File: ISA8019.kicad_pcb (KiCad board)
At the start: 2 copper layers, 157.4 x 74.2 mm, 55 parts, among them J1 Bus_ISA_16bit, J2 8P8C_Shielded, J4 JP, J5 PNP force, J6 BROM size and base address, J7 I/O base address, J8 Medium type, J9 IRQ select, T1 13F-39MNL, U1 RTL8019AS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

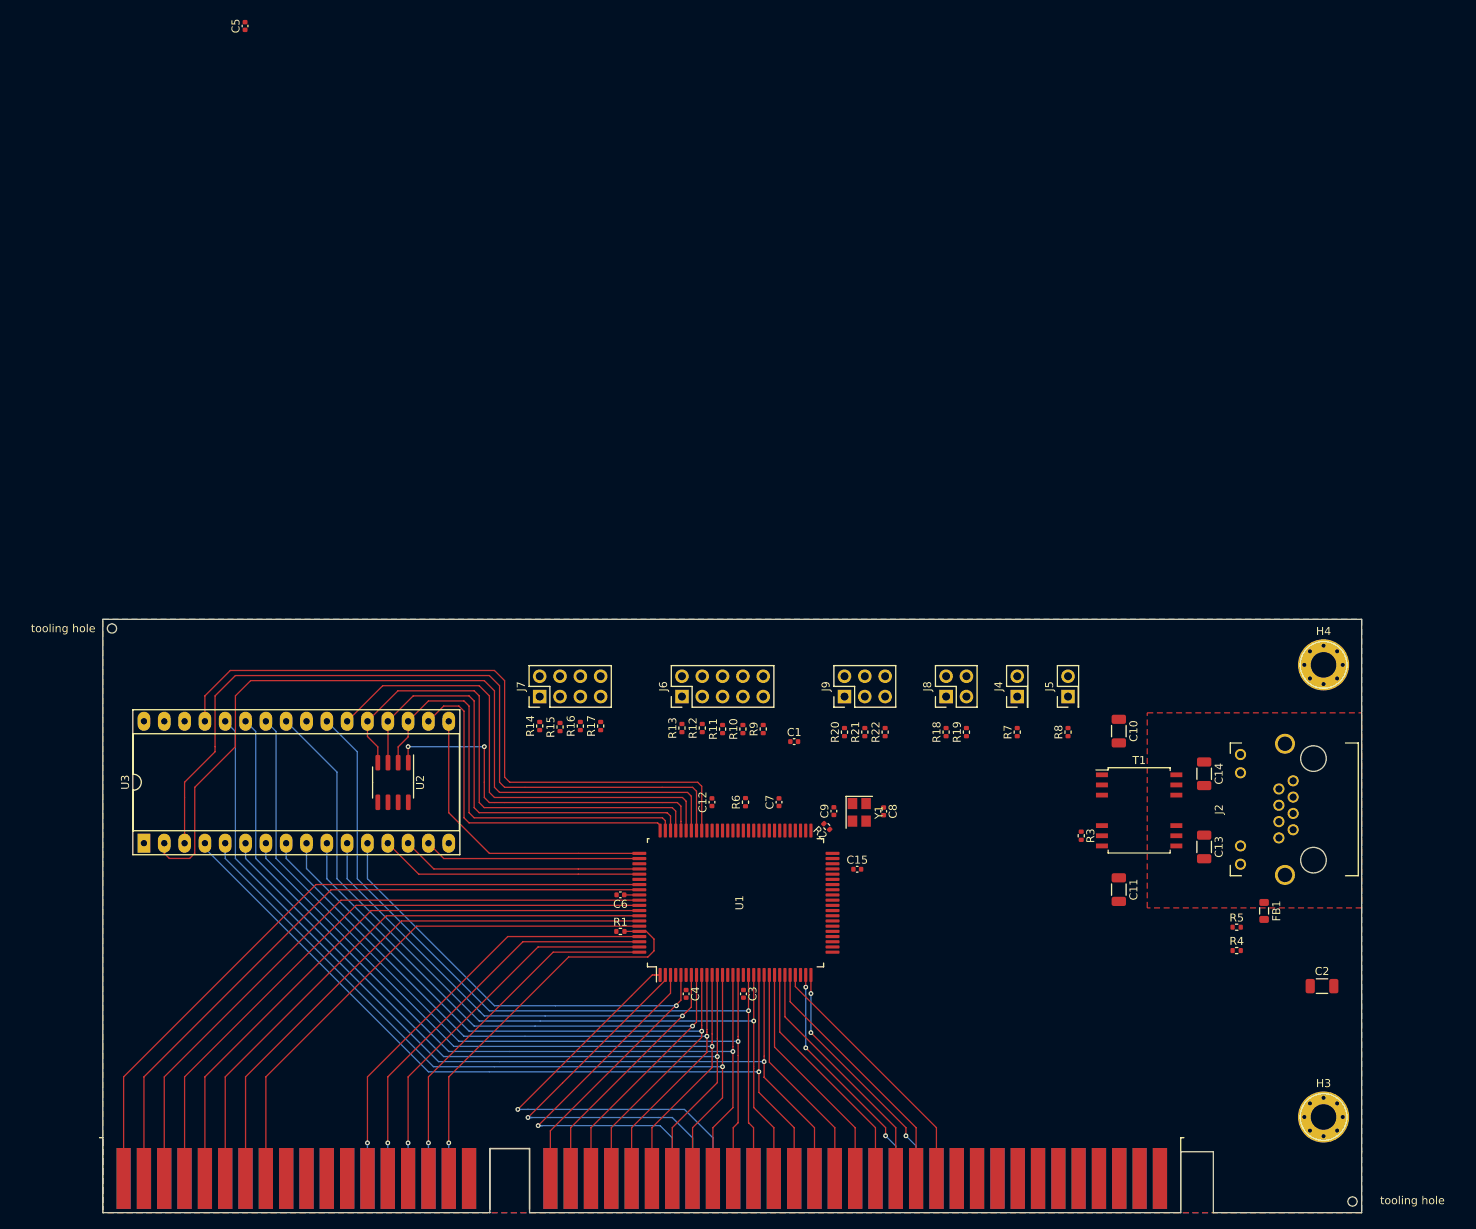
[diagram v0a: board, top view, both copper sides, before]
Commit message: Route all nets
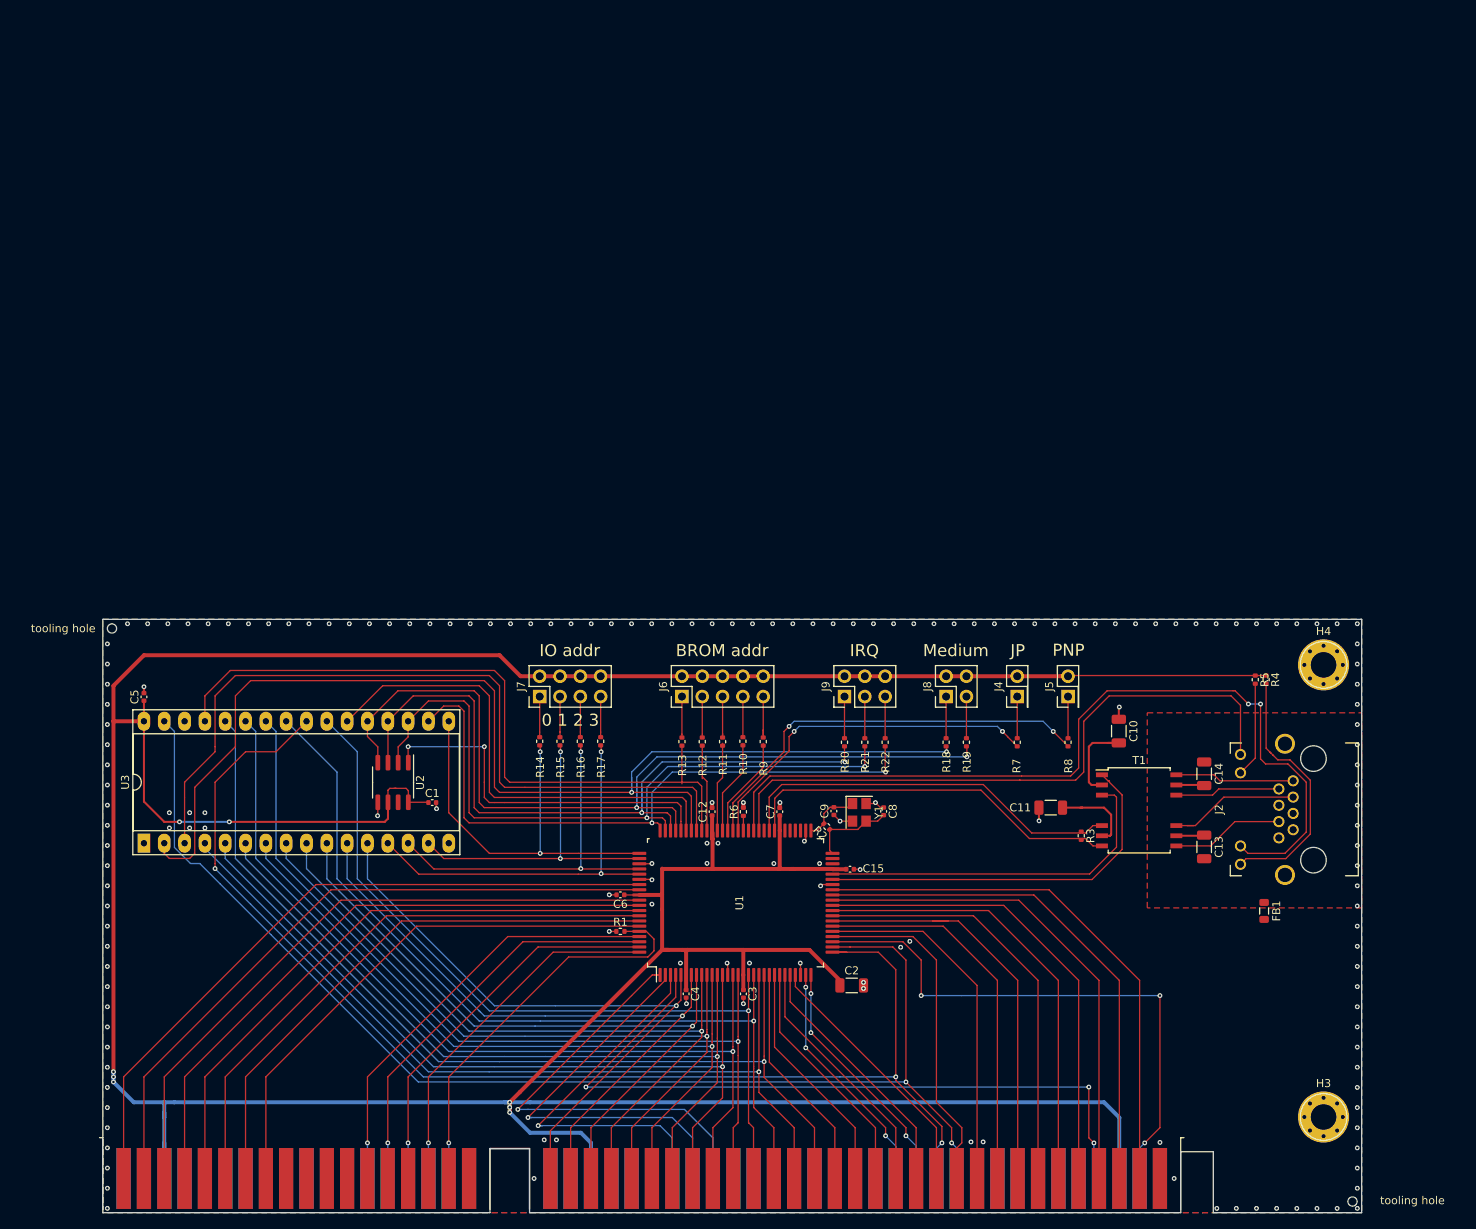
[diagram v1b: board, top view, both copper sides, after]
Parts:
- moved C5 84.8 mm to (40.7, 99.1)
- moved C2 58.8 mm to (129.2, 135.2)
- moved C1 45.9 mm to (76.7, 112.3)
- moved R4 34.1 mm to (181.0, 96.9), turned to 270 degrees
- moved R5 31.0 mm to (179.6, 96.9), turned to 270 degrees
- moved C11 13.3 mm to (154.0, 112.9), turned to 180 degrees
- moved R14 1.91 mm to (90.2, 104.6)
- moved R16 1.91 mm to (95.2, 104.6)
- moved R17 1.91 mm to (97.8, 104.6)
- moved R15 1.78 mm to (92.7, 104.7)
- moved R13 1.69 mm to (108.0, 104.7)
- moved R12 1.69 mm to (110.5, 104.7)
- moved R11 1.57 mm to (113.0, 104.7)
- moved R9 1.57 mm to (118.1, 104.7)
- moved R10 1.52 mm to (115.6, 104.6)
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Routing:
- net +5V: track 1.98 -> 539.9 mm, vias 0 -> 8
- net /~ISA_SMEMR: track 0.00 -> 161.8 mm, vias 0 -> 3
- net /~ISA_SMEMW: track 0.00 -> 159.7 mm, vias 0 -> 2
- net /LED1: track 0.00 -> 107.4 mm, vias 0 -> 2
- net /ISA_IRQ2: track 0.00 -> 93.5 mm, vias 0 -> 3
- net /LED0: track 0.00 -> 80.3 mm
- net /ISA_RESET: track 0.00 -> 70.2 mm, vias 0 -> 3
- net /ISA_D7: track 0.00 -> 67.8 mm
- net /ISA_D6: track 0.00 -> 65.0 mm
- net /ISA_D5: track 0.00 -> 62.2 mm
- net /ISA_D4: track 0.00 -> 59.4 mm
- net /ISA_D3: track 0.00 -> 56.6 mm
- net /ISA_D2: track 0.00 -> 53.8 mm
- net /ISA_D1: track 0.00 -> 52.9 mm
- net /PNP: track 0.00 -> 52.4 mm, vias 0 -> 2
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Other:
- board text added: "0 1 2 3"
- board text added: "BROM addr"
- board text added: "IO addr"
- board text added: "IRQ"
- board text added: "JP"
- board text added: "Medium"
- board text added: "PNP"

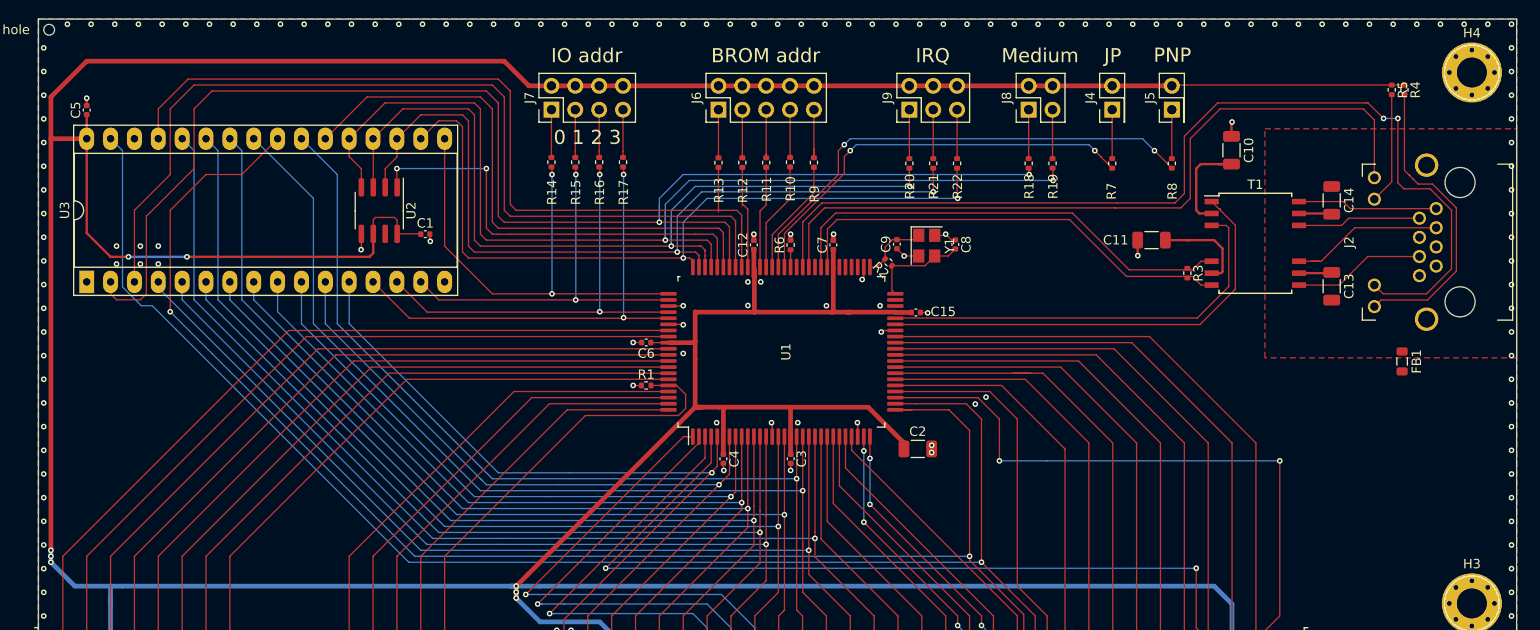
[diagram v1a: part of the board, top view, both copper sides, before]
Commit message: Add silkscreen and jumper settings
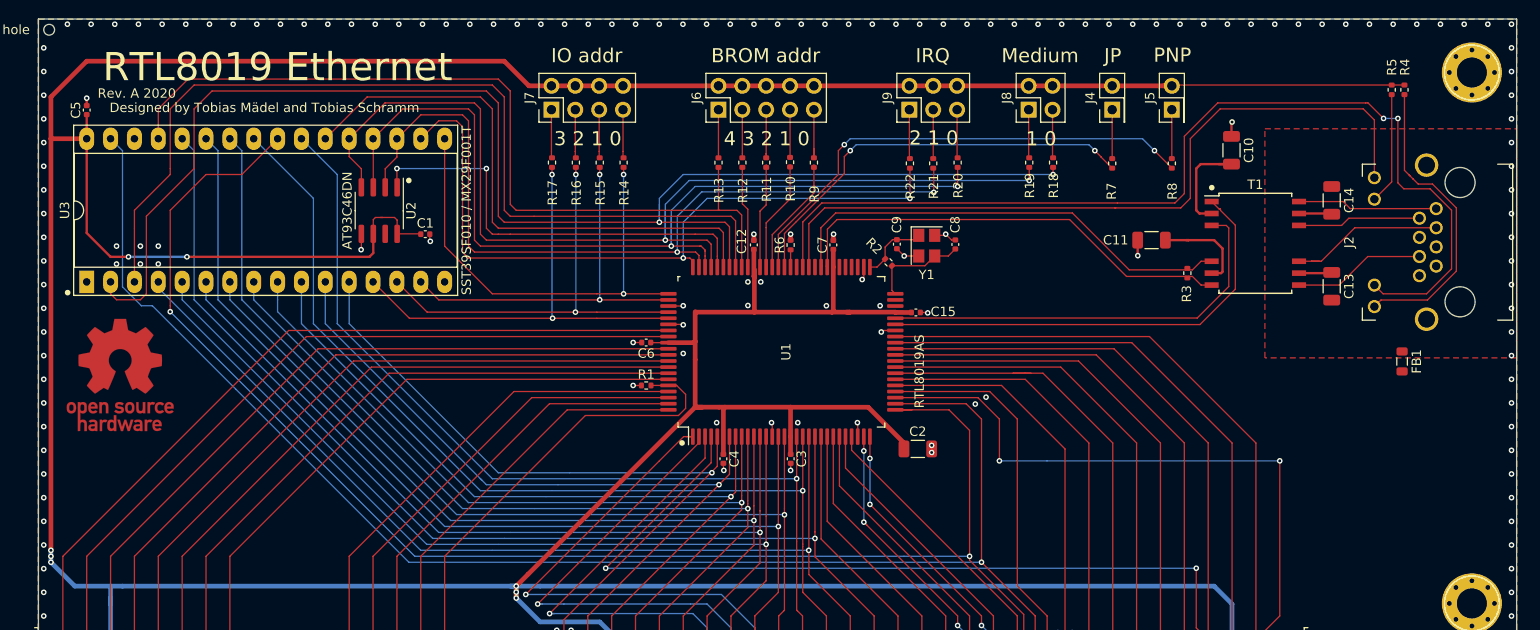
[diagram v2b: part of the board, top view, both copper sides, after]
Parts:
- added REF**: OSHW-Logo_11.4x12mm_Copper, Symbol:OSHW-Logo_11.4x12mm_Copper, F.Cu at (44.3, 127.3)
- J4: value JP -> Jumper mode
- moved R14 7.68 mm to (97.8, 104.7)
- moved R17 7.56 mm to (90.2, 104.7)
- moved R20 5.14 mm to (133.4, 104.7)
- moved R22 5.02 mm to (128.3, 104.8)
- moved R15 2.60 mm to (95.3, 104.7)
- moved R18 2.60 mm to (143.6, 104.7)
- moved R19 2.48 mm to (141.0, 104.7)
- moved R16 2.48 mm to (92.8, 104.7)
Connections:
- R14 pad 2: Net-(J7-Pad1) -> Net-(J7-Pad7)
- R15 pad 2: Net-(J7-Pad3) -> Net-(J7-Pad5)
- R16 pad 2: Net-(J7-Pad5) -> Net-(J7-Pad3)
- R17 pad 2: Net-(J7-Pad7) -> Net-(J7-Pad1)
- R18 pad 2: Net-(J8-Pad1) -> Net-(J8-Pad3)
- R19 pad 2: Net-(J8-Pad3) -> Net-(J8-Pad1)
- R20 pad 2: Net-(J9-Pad1) -> Net-(J9-Pad5)
- R22 pad 2: Net-(J9-Pad5) -> Net-(J9-Pad1)
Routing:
- net /BD6: track 93.1 -> 98.2 mm
- net /BD4: track 81.7 -> 76.6 mm
- net /BA14: track 148.1 -> 150.7 mm
- net /BD7: track 112.9 -> 110.6 mm
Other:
- board text added: "- Jumper-mode (disable PnP) - Force Plug'n'Play (ignore EEPROM settings)"
- board text added: "1 0"
- board text added: "2 1 0"
- board text added: "3 2 1 0"
- board text added: "4 3 2 1 0"
- board text added: "Boot ROM size & address 4 3 2 1 0 0 0 X X X Disabled 0 1 0 0 0 C000H, 32K 0 1 0 0 1 C800H, 32K 0 1 0 1 0 D000H, 32K 0 1 0 1 1 D800H, 32K 0 1 1 0 0 C000H, 64K 0 1 1 0 1 D000H, 64K 1 0 0 0 0 C000H, 16K 1 0 0 0 1 C400H, 16K 1 0 0 1 0 C800H, 16K 1 0 0 1 1 CC00H, 16K 1 0 1 0 0 D000H, 16K 1 0 1 0 1 D400H, 16K 1 0 1 1 0 D800H, 16K 1 0 1 1 1 DC00H, 16K 1 1 0 0 0 C000H, Paged 1 1 0 0 1 C400H, Paged 1 1 0 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"
- board text added: "Designed by Tobias Mädel and Tobias Schramm"
- board text added: "I/O address 3 2 1 0 0 0 0 0 300H 0 0 0 1 320H 0 0 1 0 340H 0 0 1 1 360H 1 0 0 0 380H 1 0 0 1 3A0H 1 0 1 0 3C0H 1 0 1 1 3E0H 0 1 0 0 200H 0 1 0 1 220H 0 1 1 0 240H 0 1 1 1 260H 1 1 0 0 280H 1 1 0 1 2A0H 1 1 1 0 2C0H 1 1 1 1 2E0H"
- board text added: "IRQ 2 1 0 0 0 0 IRQ2 0 0 1 IRQ3 0 1 0 IRQ4 0 1 1 IRQ5 1 0 0 IRQ10 1 0 1 IRQ11 1 1 0 IRQ12 1 1 1 IRQ15"
- board text added: "JP PNP Set no jumpers for PnP mode"
- board text added: "Medium type 1 0 0 0 10BaseT w/ link test 0 1 10BaseT w/o link test 1 0 10Base5 1 1 10Base2"
- board text added: "RTL8019 Ethernet"
- board text added: "Rev. A 2020"
- board text added: "tbspace.de"
- board text removed: "0 1 2 3"

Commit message: Add JLC markings, manufacturing details and new gerbers
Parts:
- removed REF**: OSHW-Logo_11.4x12mm_Copper, Symbol:OSHW-Logo_11.4x12mm_Copper
- added H5: OSHW Logo, Symbol:OSHW-Logo_11.4x12mm_Copper, F.Cu at (44.5, 127.5)
- J1: footprint Connector_PCBEdge:BUS_AT -> Bus_AT_without_Silkscreen:BUS_AT_WO_SILKSCREEN
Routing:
- net GND: track 27.1 -> 46.4 mm, vias 173 -> 218
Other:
- board text added: "JLCJLCJLCJLC"
- board text added: "JP PNP Set no jumpers for PnP mode NE2000-compatible"
- board text removed: "JP PNP Set no jumpers for PnP mode"

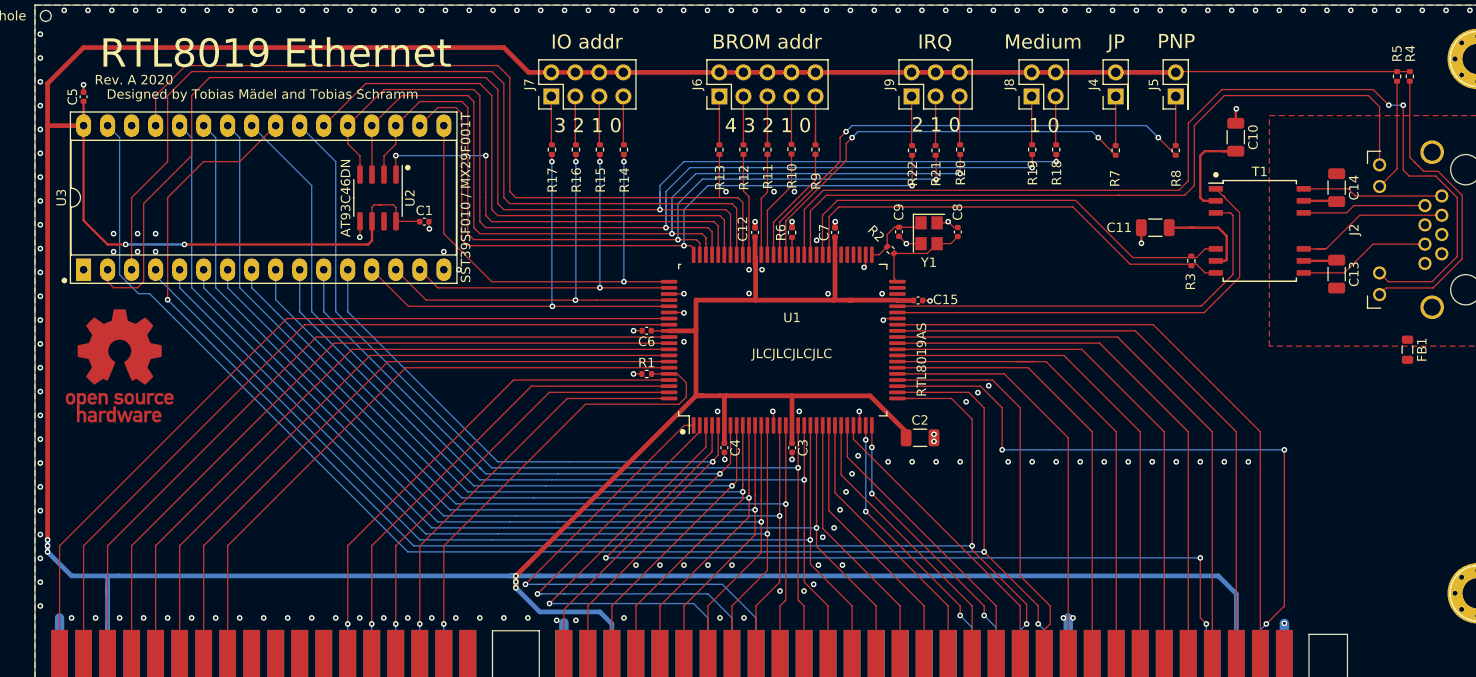
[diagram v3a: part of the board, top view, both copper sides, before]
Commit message: More GND via stitching and minor aesthetic fixes
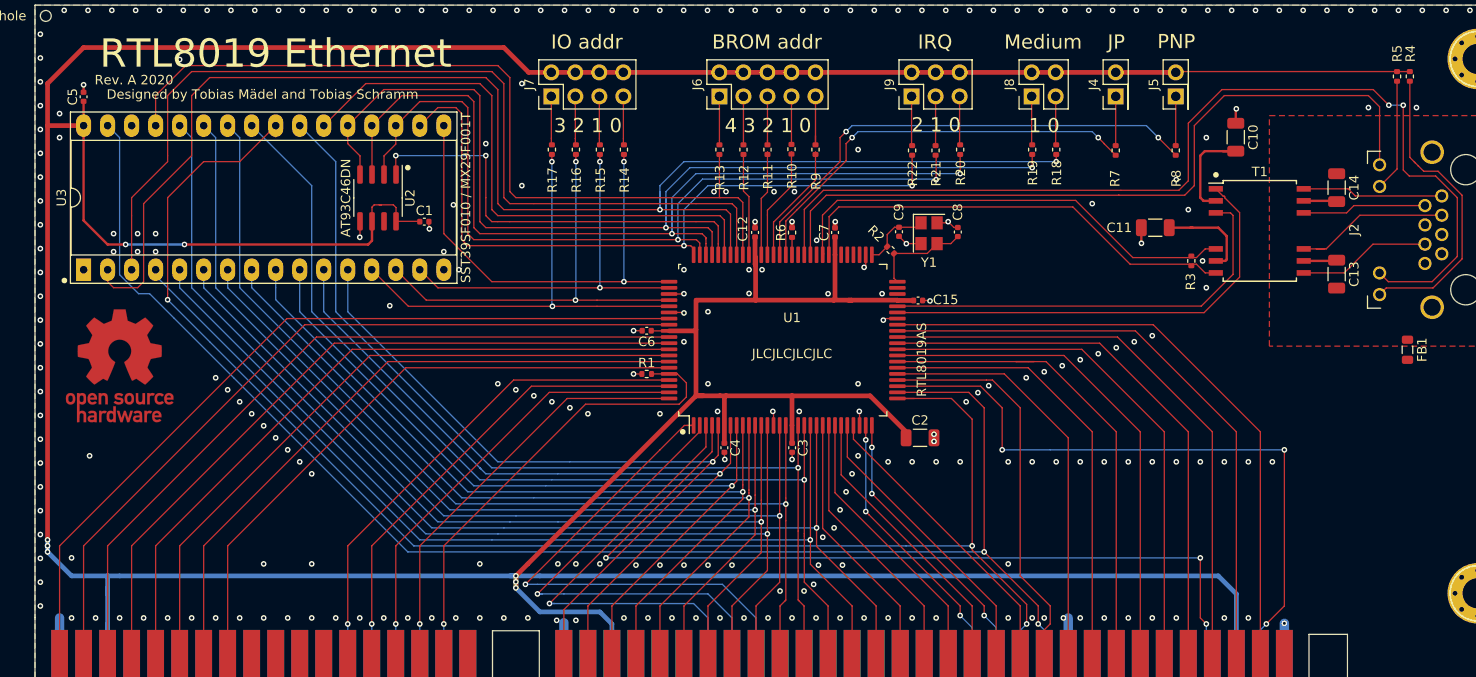
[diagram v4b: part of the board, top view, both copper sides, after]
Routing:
- net GND: vias 218 -> 294
